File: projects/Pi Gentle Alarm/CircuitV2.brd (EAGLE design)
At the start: 65 x 56 mm, 6 parts, among them X1 RASPI_BOARD_B+_E0, X2 22-23-2021

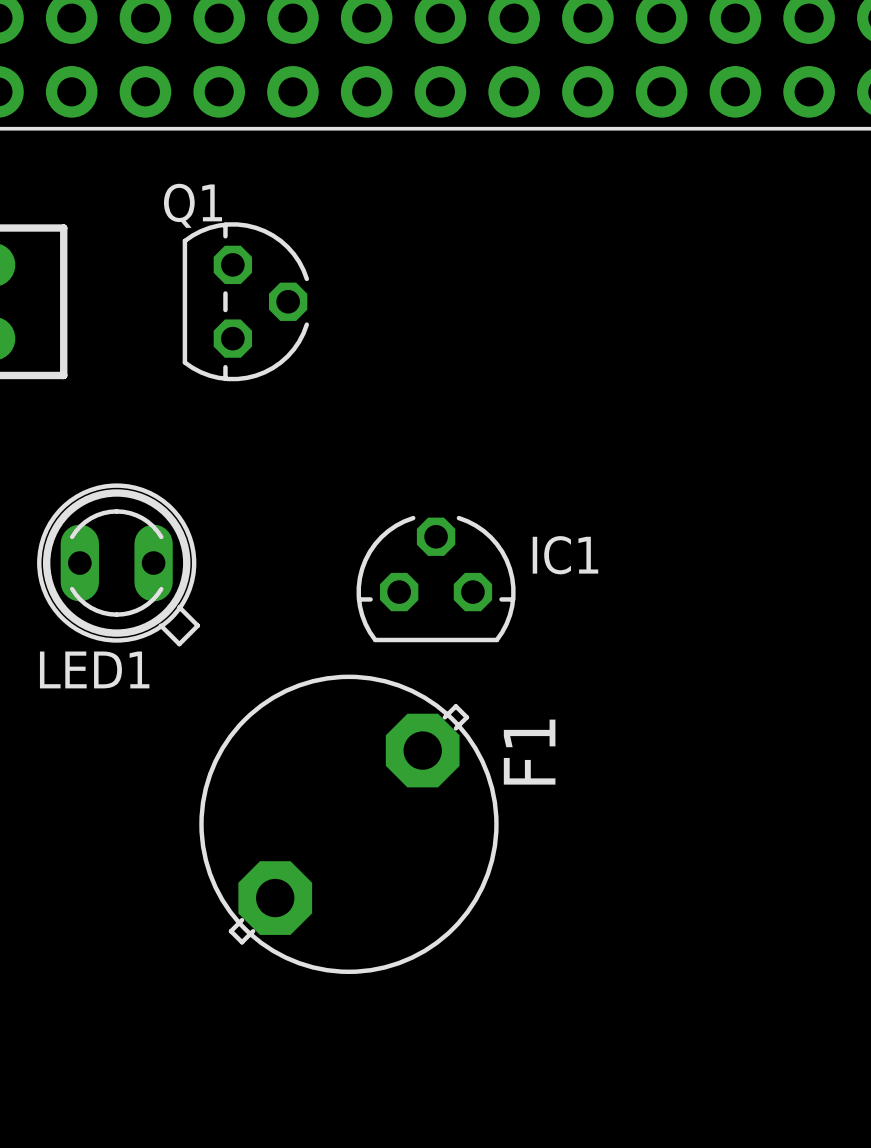
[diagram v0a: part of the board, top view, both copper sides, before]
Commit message: Changed fuse to reflect chosen model
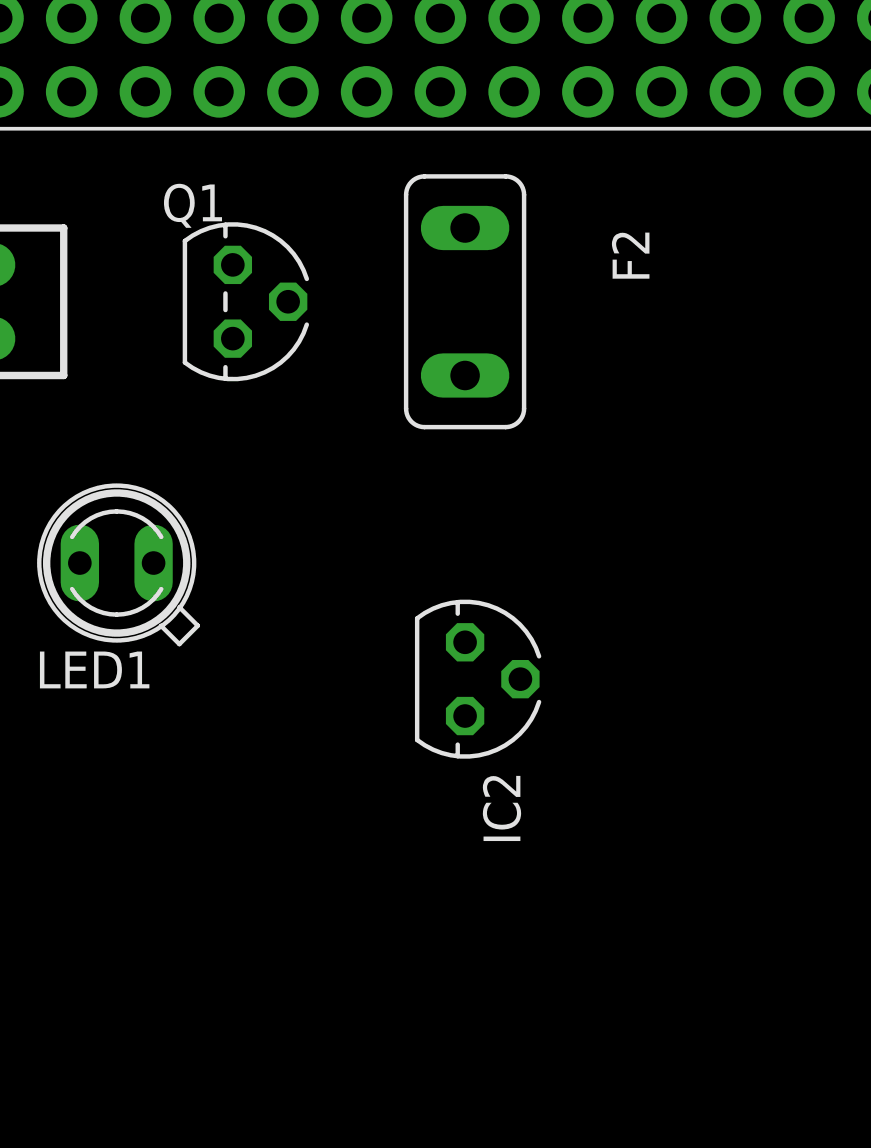
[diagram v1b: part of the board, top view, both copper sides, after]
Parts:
- removed F1: (no value), fuse:19559
- removed IC1: (no value), v-reg:78LXX
- added F2: (no value), fuse:TE5
- added IC2: (no value), v-reg:78LXX
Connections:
- net GND: now also IC2.GND; no longer IC1.GND
- net N$1: now also F2.2, IC2.OUT; no longer F1.1, IC1.IN
- net N$2: now also F2.1; no longer IC1.OUT
- net VCC: now also IC2.IN; no longer F1.2
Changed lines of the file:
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@@
 <attribute name="VALUE" x="16.27" y="39.318" size="1.27" layer="27" ratio="10" rot="R180"/>
 </element>
-<element name="IC1" library="v-reg" library_urn="urn:adsk.eagle:library:409" package="78LXX" package3d_urn="urn:adsk.eagle:package:30346/1" value="" x="26" y="34" smashed="yes">
-<attribute name="NAME" x="29.175" y="34.635" size="1.27" layer="25" ratio="10"/>
-<attribute name="POPULARITY" value="6" x="26" y="34" size="1.778" layer="27" display="off"/>
-<attribute name="VALUE" x="29.175" y="32.73" size="1.27" layer="27" ratio="10"/>
+<element name="IC2" library="v-reg" library_urn="urn:adsk.eagle:library:409" package="78LXX" package3d_urn="urn:adsk.eagle:package:30346/1" value="" x="27" y="31" smashed="yes" rot="R270">
+<attribute name="NAME" x="27.635" y="27.825" size="1.27" layer="25" ratio="10" rot="R270"/>
+<attribute name="POPULARITY" value="6" x="27" y="31" size="1.778" layer="27" rot="R270" display="off"/>
+<attribute name="VALUE" x="25.73" y="27.825" size="1.27" layer="27" ratio="10" rot="R270"/>
 </element>
-<element name="F1" library="fuse" library_urn="urn:adsk.eagle:library:233" package="19559" package3d_urn="urn:adsk.eagle:package:14056/1" value="" x="23" y="26" smashed="yes" rot="R270">
-<attribute name="MF" value="" x="23" y="26" size="1.778" layer="27" rot="R270" display="off"/>
-<attribute name="MPN" value="55900000001" x="23" y="26" size="1.778" layer="27" rot="R270" display="off"/>
-<attribute name="NAME" x="28.334" y="29.81" size="1.778" layer="25" ratio="10" rot="R270"/>
-<attribute name="OC_FARNELL" value="9516360" x="23" y="26" size="1.778" layer="27" rot="R270" display="off"/>
-<attribute name="OC_NEWARK" value="02P0286" x="23" y="26" size="1.778" layer="27" rot="R270" display="off"/>
-<attribute name="POPULARITY" value="4" x="23" y="26" size="1.778" layer="27" rot="R270" display="off"/>
-<attribute name="VALUE" x="22.111" y="30.572" size="1.778" layer="27" ratio="10" rot="R270"/>
+<element name="F2" library="fuse" library_urn="urn:adsk.eagle:library:233" package="TE5" package3d_urn="urn:adsk.eagle:package:14069/1" value="" x="27" y="44" smashed="yes" rot="R270">
+<attribute name="MF" value="" x="27" y="44" size="1.778" layer="27" rot="R270" display="off"/>
+<attribute name="MPN" value="" x="27" y="44" size="1.778" layer="27" rot="R270" display="off"/>
+<attribute name="NAME" x="32.08" y="46.54" size="1.27" layer="25" ratio="10" rot="R270"/>
+<attribute name="OC_FARNELL" value="unknown" x="27" y="44" size="1.778" layer="27" rot="R270" display="off"/>
+<attribute name="OC_NEWARK" value="unknown" x="27" y="44" size="1.778" layer="27" rot="R270" display="off"/>
+<attribute name="POPULARITY" value="0" x="27" y="44" size="1.778" layer="27" rot="R270" display="off"/>
+<attribute name="VALUE" x="24.46" y="46.54" size="1.27" layer="27" ratio="10" rot="R270"/>
 </element>
 </elements>
@@
 <contactref element="X2" pad="2"/>
 <contactref element="Q1" pad="1"/>
-<contactref element="IC1" pad="GND"/>
+<contactref element="IC2" pad="GND"/>
 </signal>
 <signal name="3V3">
@@
 <contactref element="X2" pad="1"/>
 <contactref element="LED1" pad="K"/>
-<contactref element="F1" pad="2"/>
-<wire x1="13.73" y1="35" x2="10" y2="42.73" width="0" layer="19" extent="1-1"/>
-<wire x1="20.46" y1="23.46" x2="13.73" y2="35" width="0" layer="19" extent="1-1"/>
+<contactref element="IC2" pad="IN"/>
+<wire x1="13.73" y1="35" x2="27" y2="29.73" width="0" layer="19" extent="1-1"/>
+<wire x1="10" y1="42.73" x2="13.73" y2="35" width="0" layer="19" extent="1-1"/>
 </signal>
 <signal name="GPIO17">
@@
 <signal name="N$2">
 <contactref element="X1" pad="2"/>
-<contactref element="IC1" pad="OUT"/>
-<wire x1="24.73" y1="34" x2="8.37" y2="53.77" width="0" layer="19" extent="1-1"/>
+<contactref element="F2" pad="1"/>
+<wire x1="8.37" y1="53.77" x2="27" y2="46.54" width="0" layer="19" extent="1-1"/>
 </signal>
 <signal name="N$1">
-<contactref element="IC1" pad="IN"/>
-<contactref element="F1" pad="1"/>
-<wire x1="25.54" y1="28.54" x2="27.27" y2="34" width="0" layer="19" extent="1-1"/>
+<contactref element="IC2" pad="OUT"/>
+<contactref element="F2" pad="2"/>
+<wire x1="27" y1="32.27" x2="27" y2="41.46" width="0" layer="19" extent="1-1"/>
 </signal>
 </signals>
